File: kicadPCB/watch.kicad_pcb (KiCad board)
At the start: 2 copper layers, 81 x 53 mm, 64 parts, among them IC1 ISL1209, J1 USB_OTG, M1 BOS_LIBS_SWD_BREAKOUTS, T1 BC850, U2 MKL27Z256VLH4, Y1 Crystal

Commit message: fixed pnp
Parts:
- removed T2: ~, SOT23-EBC
- added Q1: Q_PNP_CEB, TO_SOT_Packages_SMD:SOT-23, F.Cu at (162.6, 96.5)
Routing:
- net /PTC4: track 9.05 -> 7.34 mm
- net V+: track 129.6 -> 128.3 mm, vias 18 -> 19
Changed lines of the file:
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@@
     (links 159)
     (no_connects 0)
-    (area 107.917149 73.510799 191.505 131.576618)
+    (area 107.917149 78.430582 189.085051 131.576618)
     (thickness 1.6)
     (drawings 84)
-    (tracks 863)
+    (tracks 861)
     (zones 0)
     (modules 64)
@@
       (net 52 /N$42))
   )
-  (module SOT23-EBC (layer Top)
-    (at 162.730244 96.660589 270)
-    (descr "<b>SOT-23 (EBC)</b>")
-    (fp_text reference T2 (at -1.905 -1.905 270) (layer F.SilkS)
-      (effects (font (size 1.2065 1.2065) (thickness 0.1016)) (justify right top))
-    )
-    (fp_text value ~ (at -1.905 3.175 270) (layer F.SilkS)
-      (effects (font (size 1.2065 1.2065) (thickness 0.1016)) (justify right top))
-    )
-    (fp_line (start 1.4224 -0.6604) (end 1.4224 0.6604) (layer Dwgs.User) (width 0.127))
-    (fp_line (start 1.4224 0.6604) (end -1.4224 0.6604) (layer Dwgs.User) (width 0.127))
-    (fp_line (start -1.4224 0.6604) (end -1.4224 -0.6604) (layer Dwgs.User) (width 0.127))
-    (fp_line (start -1.4224 -0.6604) (end 1.4224 -0.6604) (layer Dwgs.User) (width 0.127))
-    (fp_poly (pts (xy -0.2286 -0.7112) (xy 0.2286 -0.7112) (xy 0.2286 -1.2954) (xy -0.2286 -1.2954)) (layer Dwgs.User) (width 0))
-    (fp_poly (pts (xy 0.7112 1.2954) (xy 1.1684 1.2954) (xy 1.1684 0.7112) (xy 0.7112 0.7112)) (layer Dwgs.User) (width 0))
-    (fp_poly (pts (xy -1.1684 1.2954) (xy -0.7112 1.2954) (xy -0.7112 0.7112) (xy -1.1684 0.7112)) (layer Dwgs.User) (width 0))
-    (pad C smd rect (at 0 -1.1 270) (size 1 1.4) (layers Top F.Paste F.Mask)
-      (net 4 /N$6))
-    (pad B smd rect (at 0.95 1.1 270) (size 1 1.4) (layers Top F.Paste F.Mask)
-      (net 59 /PTC4))
-    (pad E smd rect (at -0.95 1.1 270) (size 1 1.4) (layers Top F.Paste F.Mask)
-      (net 2 V+))
-  )
   (module SOT23-5 (layer Top)
     (at 172.382244 85.865589 90)
@@
       (net 124 "Net-(J1-Pad6)"))
   )
+  (module TO_SOT_Packages_SMD:SOT-23 (layer Top)
+    (at 162.56 96.52)
+    (descr "SOT-23, Standard")
+    (tags SOT-23)
+    (attr smd)
+    (fp_text reference Q1 (at 0 -2.5) (layer F.SilkS)
+      (effects (font (size 1 1) (thickness 0.15)))
+    )
+    (fp_text value Q_PNP_CEB (at 0 2.5) (layer F.Fab)
+      (effects (font (size 1 1) (thickness 0.15)))
+    )
+    (fp_line (start 0.76 1.58) (end 0.76 0.65) (layer F.SilkS) (width 0.12))
+    (fp_line (start 0.76 -1.58) (end 0.76 -0.65) (layer F.SilkS) (width 0.12))
+    (fp_line (start 0.7 -1.52) (end 0.7 1.52) (layer F.Fab) (width 0.15))
+    (fp_line (start -0.7 1.52) (end 0.7 1.52) (layer F.Fab) (width 0.15))
+    (fp_line (start -1.7 -1.75) (end 1.7 -1.75) (layer F.CrtYd) (width 0.05))
+    (fp_line (start 1.7 -1.75) (end 1.7 1.75) (layer F.CrtYd) (width 0.05))
+    (fp_line (start 1.7 1.75) (end -1.7 1.75) (layer F.CrtYd) (width 0.05))
+    (fp_line (start -1.7 1.75) (end -1.7 -1.75) (layer F.CrtYd) (width 0.05))
+    (fp_line (start 0.76 -1.58) (end -1.4 -1.58) (layer F.SilkS) (width 0.12))
+    (fp_line (start -0.7 -1.52) (end 0.7 -1.52) (layer F.Fab) (width 0.15))
+    (fp_line (start -0.7 -1.52) (end -0.7 1.52) (layer F.Fab) (width 0.15))
+    (fp_line (start 0.76 1.58) (end -0.7 1.58) (layer F.SilkS) (width 0.12))
+    (pad 1 smd rect (at -1 -0.95) (size 0.9 0.8) (layers Top F.Paste F.Mask)
+      (net 59 /PTC4))
+    (pad 2 smd rect (at -1 0.95) (size 0.9 0.8) (layers Top F.Paste F.Mask)
+      (net 2 V+))
+    (pad 3 smd rect (at 1 0) (size 0.9 0.8) (layers Top F.Paste F.Mask)
+      (net 4 /N$6))
+    (model TO_SOT_Packages_SMD.3dshapes/SOT-23.wrl
+      (at (xyz 0 0 0))
+      (scale (xyz 1 1 1))
+      (rotate (xyz 0 0 90))
+    )
+  )
   (gr_text "IR LED" (at 137.16 80.772) (layer F.SilkS)
     (effects (font (size 0.5 0.5) (thickness 0.125)))
@@
   (segment (start 155.745244 92.850589) (end 156.761244 93.739589) (width 0.254) (layer Bottom) (net 1))
   (segment (start 156.761244 93.739589) (end 156.761244 95.009589) (width 0.254) (layer Bottom) (net 1))
+  (via (at 158.75 96.52) (size 0.6) (drill 0.4) (layers Top Bottom) (net 2))
+  (segment (start 160.56 96.52) (end 158.75 96.52) (width 0.25) (layer Top) (net 2))
+  (segment (start 161.56 97.47) (end 161.51 97.47) (width 0.25) (layer Top) (net 2))
+  (segment (start 161.51 97.47) (end 160.56 96.52) (width 0.25) (layer Top) (net 2))
+  (segment (start 161.56 97.395345) (end 161.56 97.47) (width 0.25) (layer Top) (net 2))
   (segment (start 116.756244 111.812589) (end 120.618833 107.95) (width 0.25) (layer Bottom) (net 2))
   (segment (start 120.618833 107.95) (end 126.365 107.95) (width 0.25) (layer Bottom) (net 2))
@@
   (segment (start 155.602897 99.088936) (end 154.373378 97.859417) (width 0.3048) (layer Top) (net 2))
   (segment (start 156.507244 100.501283) (end 156.761244 100.978589) (width 0.3048) (layer Top) (net 2))
-  (segment (start 158.966144 93.469589) (end 159.682244 94.185689) (width 0.254) (layer Top) (net 2))
   (segment (start 169.581244 98.093589) (end 168.227244 98.093589) (width 0.254) (layer Top) (net 2))
   (segment (start 168.227244 98.093589) (end 167.302244 97.168589) (width 0.254) (layer Top) (net 2))
@@
   (segment (start 157.650244 93.485589) (end 158.950144 93.485589) (width 0.254) (layer Top) (net 2))
   (segment (start 158.950144 93.485589) (end 158.966144 93.469589) (width 0.254) (layer Top) (net 2))
-  (segment (start 159.682244 94.185689) (end 159.682244 94.755589) (width 0.254) (layer Top) (net 2))
-  (segment (start 159.682244 94.755589) (end 160.444244 95.517589) (width 0.254) (layer Top) (net 2))
-  (segment (start 160.444244 95.517589) (end 161.945244 95.517589) (width 0.254) (layer Top) (net 2))
-  (segment (start 161.945244 95.517589) (end 161.630244 95.710589) (width 0.254) (layer Top) (net 2))
   (segment (start 123.233244 94.667589) (end 124.845244 94.667589) (width 0.254) (layer Top) (net 2))
   (segment (start 124.845244 94.667589) (end 125.011244 94.501589) (width 0.254) (layer Top) (net 2))
@@
   (segment (start 127.805244 91.072589) (end 128.694244 91.072589) (width 0.254) (layer Bottom) (net 58))
   (segment (start 123.106244 86.500589) (end 127.805244 91.072589) (width 0.254) (layer Bottom) (net 58))
-  (segment (start 161.630244 97.610589) (end 160.505244 97.483589) (width 0.254) (layer Top) (net 59))
-  (segment (start 154.373378 95.207764) (end 155.079553 94.501589) (width 0.254) (layer Top) (net 59))
-  (segment (start 155.079553 94.501589) (end 158.285244 94.501589) (width 0.254) (layer Top) (net 59))
-  (segment (start 158.285244 94.501589) (end 160.505244 97.483589) (width 0.254) (layer Top) (net 59))
+  (segment (start 161.56 95.57) (end 154.735615 95.57) (width 0.25) (layer Top) (net 59))
+  (segment (start 154.735615 95.57) (end 154.373379 95.207764) (width 0.25) (layer Top) (net 59))
   (segment (start 112.44 105.27) (end 113.19 105.27) (width 0.25) (layer Top) (net 60))
   (segment (start 117.64 99.22) (end 117.64 98.47) (width 0.25) (layer Top) (net 60))

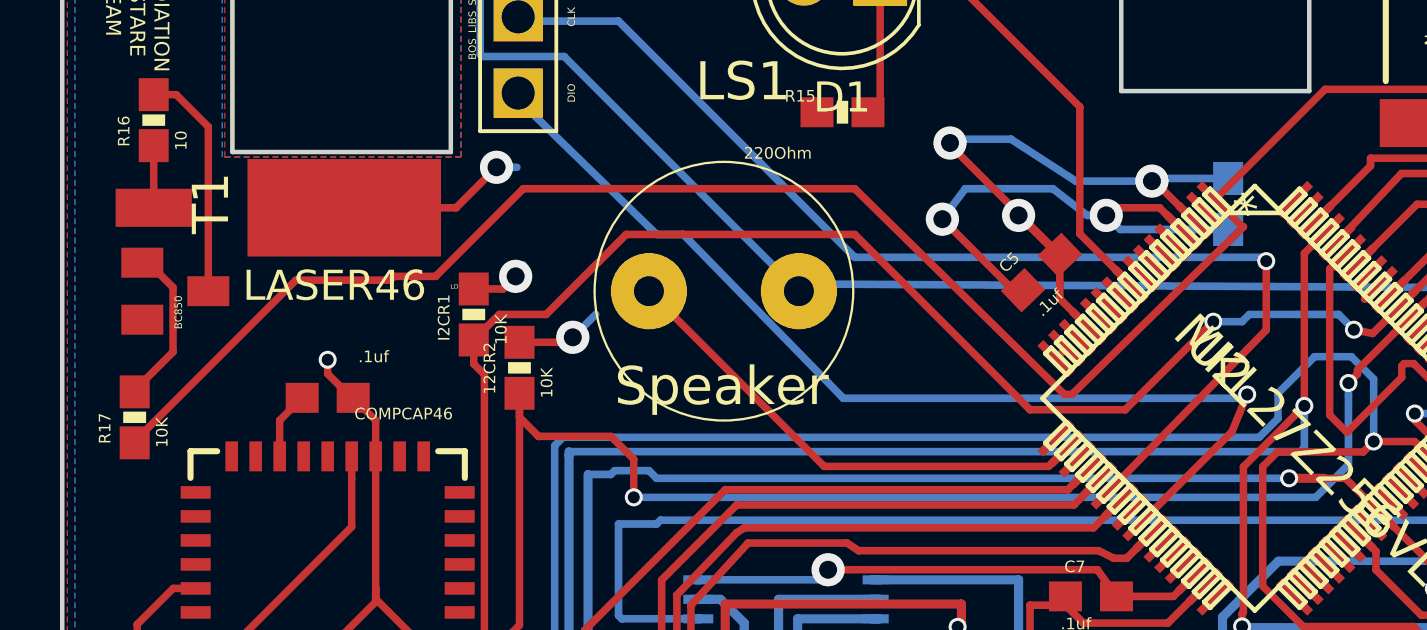
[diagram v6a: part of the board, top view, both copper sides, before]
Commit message: fixed Laser npn, fixed laser and led south from bridge
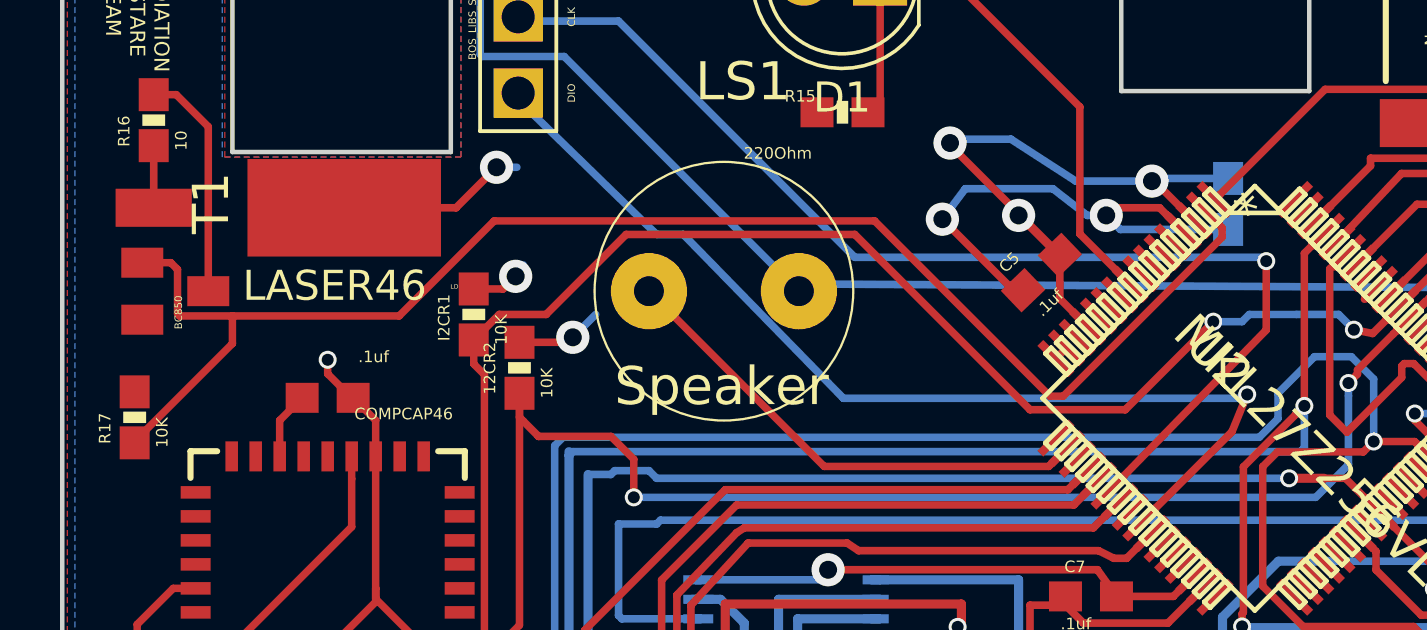
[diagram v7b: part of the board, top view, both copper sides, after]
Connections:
- R17 pad 1: /PTE0 -> /PTE1
- R17 pad 2: /N$42 -> GND
- T1 pad 1: /N$42 -> /PTE1
- U2 pad 2: Net-(U2-Pad2) -> /PTE1
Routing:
- net /PTE1: track 0.00 -> 50.5 mm
- net /PTE0: track 112.2 -> 65.3 mm
- net /N$42: track 5.46 -> 0.00 mm
